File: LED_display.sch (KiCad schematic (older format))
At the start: 22 parts, among them J1 Conn_01x08_Male, J2 Conn_01x08_Male, J8 Conn_01x08_Male, J9 Conn_01x08_Male

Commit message: Tidy schematic / renumber components / complete daughter boards
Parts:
- added J22, J24: ~, Connector_PinSocket_2.54mm:PinSocket_1x08_P2.54mm_Vertical, symbol Connector:Conn_01x08_Female
- added J25, J27: ~, Connector_PinHeader_2.54mm:PinHeader_1x08_P2.54mm_Vertical, symbol Connector:Conn_01x08_Male
- D1, D10, D11, D12, D13, D14, D15, D16, D2, D3, D4, D5, D6, D7, D8, D9: value ~ -> LED
- J21: renamed from J1; value Conn_01x08_Male -> ~
- J23: renamed from J2; value Conn_01x08_Male -> ~
- J26: renamed from J8; value Conn_01x08_Male -> ~; footprint Connector_PinHeader_2.54mm:PinHeader_1x08_P2.54mm_Vertical -> Connector_PinSocket_2.54mm:PinSocket_1x08_P2.54mm_Vertical; symbol Connector:Conn_01x08_Male -> Connector:Conn_01x08_Female
- J28: renamed from J9; value Conn_01x08_Male -> ~; footprint Connector_PinHeader_2.54mm:PinHeader_1x08_P2.54mm_Vertical -> Connector_PinSocket_2.54mm:PinSocket_1x08_P2.54mm_Vertical; symbol Connector:Conn_01x08_Male -> Connector:Conn_01x08_Female
- RN2, RN3: value R_Network08 -> 680Ω (Bussed)
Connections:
- net LED_1: now also J22.1 (Pin_1); no longer D1.2 (A), J21.1 (Pin_1)
- net LED_10: now also J24.2 (Pin_2); no longer D10.2 (A), J23.2 (Pin_2)
- net LED_11: now also J24.3 (Pin_3); no longer D11.2 (A), J23.3 (Pin_3)
- net LED_12: now also J24.4 (Pin_4); no longer D12.2 (A), J23.4 (Pin_4)
- net LED_13: now also J24.5 (Pin_5); no longer D13.2 (A), J23.5 (Pin_5)
- net LED_14: now also J24.6 (Pin_6); no longer D14.2 (A), J23.6 (Pin_6)
- net LED_15: now also J24.7 (Pin_7); no longer D15.2 (A), J23.7 (Pin_7)
- net LED_16: now also J24.8 (Pin_8); no longer D16.2 (A), J23.8 (Pin_8)
- net LED_2: now also J22.2 (Pin_2); no longer D2.2 (A), J21.2 (Pin_2)
- net LED_3: now also J22.3 (Pin_3); no longer D3.2 (A), J21.3 (Pin_3)
- net LED_4: now also J22.4 (Pin_4); no longer D4.2 (A), J21.4 (Pin_4)
- net LED_5: now also J22.5 (Pin_5); no longer D5.2 (A), J21.5 (Pin_5)
- net LED_6: now also J22.6 (Pin_6); no longer D6.2 (A), J21.6 (Pin_6)
- net LED_7: now also J22.7 (Pin_7); no longer D7.2 (A), J21.7 (Pin_7)
- net LED_8: now also J22.8 (Pin_8); no longer D8.2 (A), J21.8 (Pin_8)
- net LED_9: now also J24.1 (Pin_1); no longer D9.2 (A), J23.1 (Pin_1)
- net at J26.5 (Pin_5), RN2.6 (R5): no longer D5.1 (K)
- net at J26.6 (Pin_6), RN2.7 (R6): no longer D6.1 (K)
- net at J26.7 (Pin_7), RN2.8 (R7): no longer D7.1 (K)
- net at J26.4 (Pin_4), RN2.5 (R4): no longer D4.1 (K)
- net at J26.3 (Pin_3), RN2.4 (R3): no longer D3.1 (K)
- net at J26.2 (Pin_2), RN2.3 (R2): no longer D2.1 (K)
- net at J26.8 (Pin_8), RN2.9 (R8): no longer D8.1 (K)
- net at J28.1 (Pin_1), RN3.2 (R1): no longer D9.1 (K)
- net at J26.1 (Pin_1), RN2.2 (R1): no longer D1.1 (K)
- net at J28.6 (Pin_6), RN3.7 (R6): no longer D14.1 (K)
- net at J28.7 (Pin_7), RN3.8 (R7): no longer D15.1 (K)
- net at J28.8 (Pin_8), RN3.9 (R8): no longer D16.1 (K)
- net at J28.5 (Pin_5), RN3.6 (R5): no longer D13.1 (K)
- net at J28.4 (Pin_4), RN3.5 (R4): no longer D12.1 (K)
- net at J28.3 (Pin_3), RN3.4 (R3): no longer D11.1 (K)
- net at J28.2 (Pin_2), RN3.3 (R2): no longer D10.1 (K)
- new net: D5.1 (K), J25.5 (Pin_5)
- new net: D5.2 (A), J21.5 (Pin_5)
- new net: D6.1 (K), J25.6 (Pin_6)
- new net: D6.2 (A), J21.6 (Pin_6)
- new net: D7.1 (K), J25.7 (Pin_7)
- new net: D7.2 (A), J21.7 (Pin_7)
- new net: D4.1 (K), J25.4 (Pin_4)
- new net: D4.2 (A), J21.4 (Pin_4)
- new net: D3.1 (K), J25.3 (Pin_3)
- new net: D3.2 (A), J21.3 (Pin_3)
- new net: D2.1 (K), J25.2 (Pin_2)
- new net: D2.2 (A), J21.2 (Pin_2)
- new net: D8.1 (K), J25.8 (Pin_8)
- new net: D8.2 (A), J21.8 (Pin_8)
- new net: D9.1 (K), J27.1 (Pin_1)
- new net: D9.2 (A), J23.1 (Pin_1)
- new net: D1.1 (K), J25.1 (Pin_1)
- new net: D1.2 (A), J21.1 (Pin_1)
- new net: D14.1 (K), J27.6 (Pin_6)
- new net: D14.2 (A), J23.6 (Pin_6)
- new net: D15.1 (K), J27.7 (Pin_7)
- new net: D15.2 (A), J23.7 (Pin_7)
- new net: D16.1 (K), J27.8 (Pin_8)
- new net: D16.2 (A), J23.8 (Pin_8)
- new net: D13.1 (K), J27.5 (Pin_5)
- new net: D13.2 (A), J23.5 (Pin_5)
- new net: D12.1 (K), J27.4 (Pin_4)
- new net: D12.2 (A), J23.4 (Pin_4)
- new net: D11.1 (K), J27.3 (Pin_3)
- new net: D11.2 (A), J23.3 (Pin_3)
- new net: D10.1 (K), J27.2 (Pin_2)
- new net: D10.2 (A), J23.2 (Pin_2)
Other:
- note added: "Board Separator"
- note removed: "Display block"
- moved on the sheet: D1, D10, D11, D12, D13, D14, D15, D16, D2, D3, D4, D5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

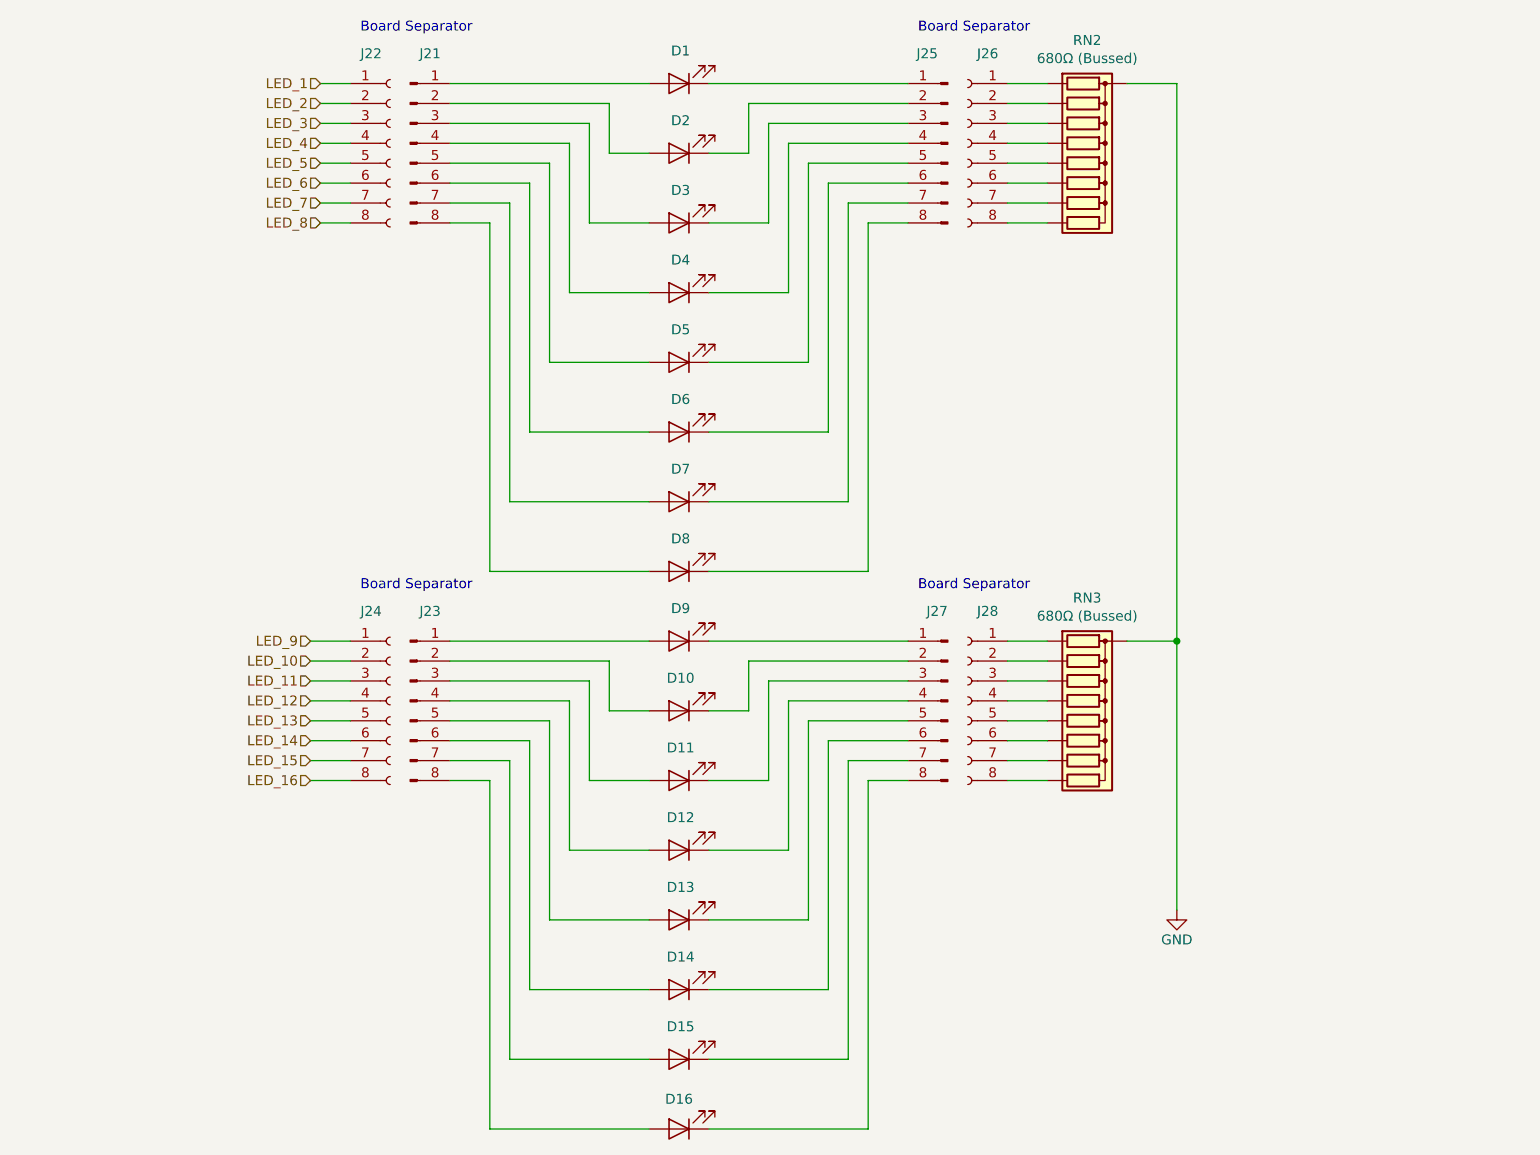
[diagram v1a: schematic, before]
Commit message: Further cleanup and placement
Removed all the connectors to the rails as they're irrelevant to the top boards.

Added all the support headers.

Need to work out the correct routing for the headers but the placement is correct.
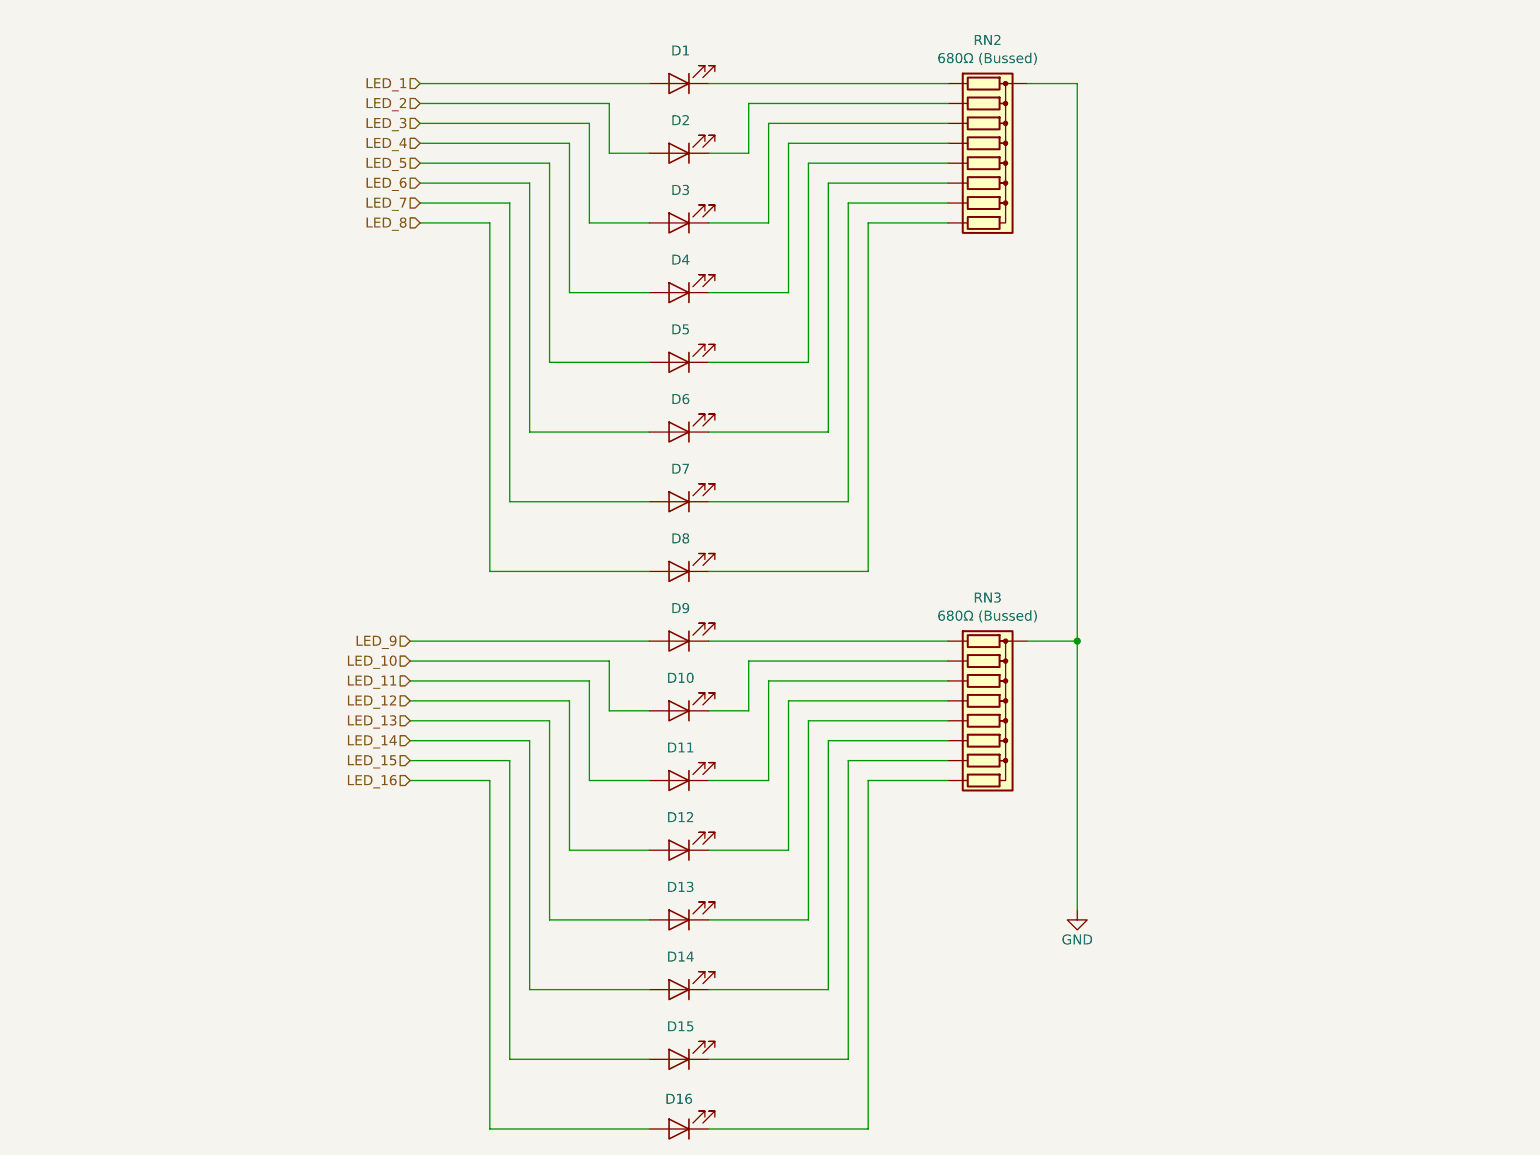
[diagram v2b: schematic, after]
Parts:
- removed J21, J23, J25, J27: ~, Connector_PinHeader_2.54mm:PinHeader_1x08_P2.54mm_Vertical, symbol Connector:Conn_01x08_Male
- removed J22, J24, J26, J28: ~, Connector_PinSocket_2.54mm:PinSocket_1x08_P2.54mm_Vertical, symbol Connector:Conn_01x08_Female
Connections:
- net LED_1: now also D1.2 (A)
- net LED_10: now also D10.2 (A)
- net LED_11: now also D11.2 (A)
- net LED_12: now also D12.2 (A)
- net LED_13: now also D13.2 (A)
- net LED_14: now also D14.2 (A)
- net LED_15: now also D15.2 (A)
- net LED_16: now also D16.2 (A)
- net LED_2: now also D2.2 (A)
- net LED_3: now also D3.2 (A)
- net LED_4: now also D4.2 (A)
- net LED_5: now also D5.2 (A)
- net LED_6: now also D6.2 (A)
- net LED_7: now also D7.2 (A)
- net LED_8: now also D8.2 (A)
- net LED_9: now also D9.2 (A)
- net at D5.1 (K): now also RN2.6 (R5)
- net at D6.1 (K): now also RN2.7 (R6)
- net at D7.1 (K): now also RN2.8 (R7)
- net at D4.1 (K): now also RN2.5 (R4)
- net at D3.1 (K): now also RN2.4 (R3)
- net at D2.1 (K): now also RN2.3 (R2)
- net at D8.1 (K): now also RN2.9 (R8)
- net at D9.1 (K): now also RN3.2 (R1)
- net at D1.1 (K): now also RN2.2 (R1)
- net at D14.1 (K): now also RN3.7 (R6)
- net at D15.1 (K): now also RN3.8 (R7)
- net at D16.1 (K): now also RN3.9 (R8)
- net at D13.1 (K): now also RN3.6 (R5)
- net at D12.1 (K): now also RN3.5 (R4)
- net at D11.1 (K): now also RN3.4 (R3)
- net at D10.1 (K): now also RN3.3 (R2)
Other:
- note removed: "Board Separator"
- moved on the sheet: RN2, RN3

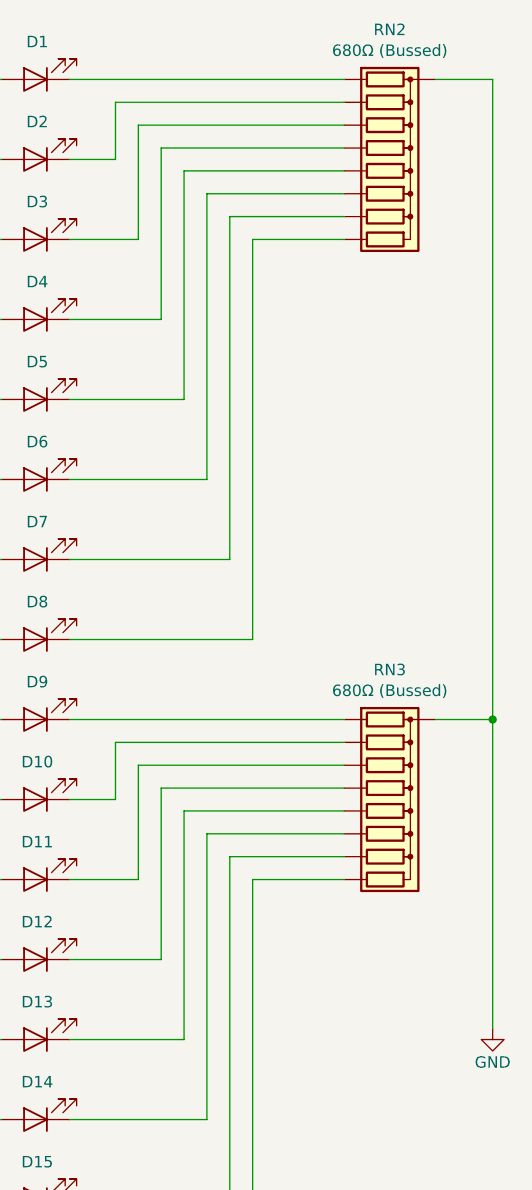
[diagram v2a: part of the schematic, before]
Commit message: Moved two overlapping boards out of the way for clarity and cleaned up folder
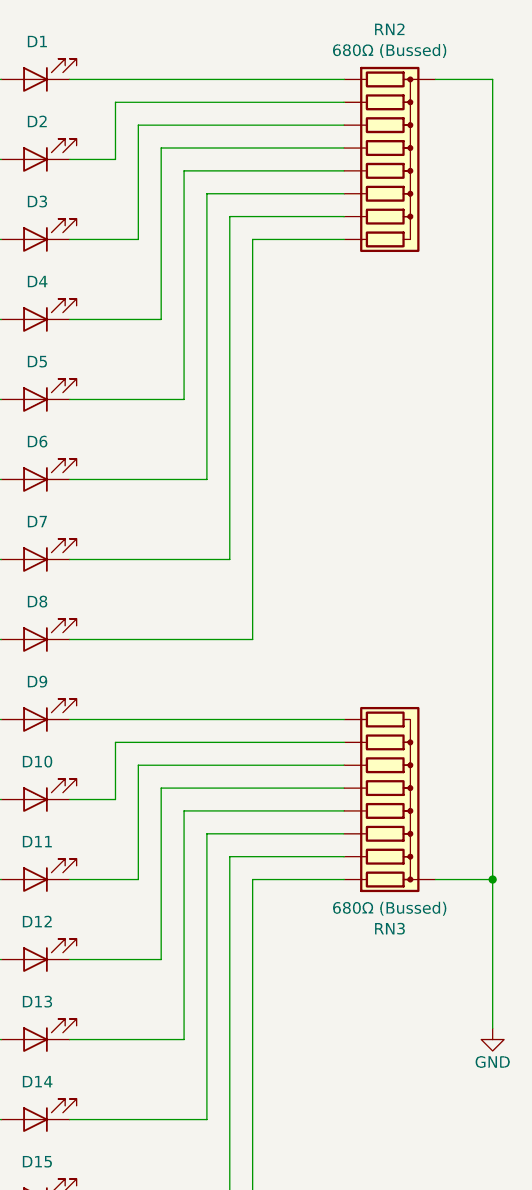
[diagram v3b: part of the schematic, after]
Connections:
- net at D9.1 (K): now also RN3.9 (R8); no longer RN3.2 (R1)
- net at D14.1 (K): now also RN3.4 (R3); no longer RN3.7 (R6)
- net at D15.1 (K): now also RN3.3 (R2); no longer RN3.8 (R7)
- net at D16.1 (K): now also RN3.2 (R1); no longer RN3.9 (R8)
- net at D13.1 (K): now also RN3.5 (R4); no longer RN3.6 (R5)
- net at D12.1 (K): now also RN3.6 (R5); no longer RN3.5 (R4)
- net at D11.1 (K): now also RN3.7 (R6); no longer RN3.4 (R3)
- net at D10.1 (K): now also RN3.8 (R7); no longer RN3.3 (R2)
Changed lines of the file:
@@
 L Device:R_Network08 RN3
 U 1 1 5C58845F
-P 5550 4650
-F 0 "RN3" V 4933 4650 50  0000 C CNN
-F 1 "680Ω (Bussed)" V 5024 4650 50  0000 C CNN
-F 2 "Resistor_THT:R_Array_SIP9" V 6025 4650 50  0001 C CNN
-F 3 "http://www.vishay.com/docs/31509/csc.pdf" H 5550 4650 50  0001 C CNN
-	1    5550 4650
-	0    1    1    0
+P 5550 4550
+F 0 "RN3" V 4933 4550 50  0000 C CNN
+F 1 "680Ω (Bussed)" V 5024 4550 50  0000 C CNN
+F 2 "Resistor_THT:R_Array_SIP9" V 6025 4550 50  0001 C CNN
+F 3 "http://www.vishay.com/docs/31509/csc.pdf" H 5550 4550 50  0001 C CNN
+	1    5550 4550
+	0    1    -1   0
 $EndComp
-Wire Wire Line
-	5750 4250 6000 4250
 Wire Wire Line
 	5750 1450 6000 1450
@@
 Wire Wire Line
 	4950 3900 4950 2150
-Wire Wire Line
-	6000 1450 6000 4250
-Connection ~ 6000 4250
-Wire Wire Line
-	6000 4250 6000 5600
 Wire Wire Line
 	4150 4600 4350 4600
@@
 Wire Wire Line
 	4150 4250 5350 4250
+Wire Wire Line
+	5750 4950 6000 4950
+Connection ~ 6000 4950
+Wire Wire Line
+	6000 4950 6000 5600
+Wire Wire Line
+	6000 1450 6000 4950
 $EndSCHEMATC
